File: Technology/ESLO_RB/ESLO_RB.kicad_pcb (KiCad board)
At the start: 4 copper layers, 48.8 x 20 mm, 71 parts, among them J1 Board to Board, J2 Conn_01x10_Female, U1 TPS62740, U10 MT29F2G01ABBGDWB-IT:G TR, U2 LP5907MFX-1.5, U3 CC2652RB, U4 2450BM14G0011, U5 MAX1720, U6 TPS72301DDCT, U7 ADS1294, U8 LSM303AGR, U9 CY15V104QI-20LPXC

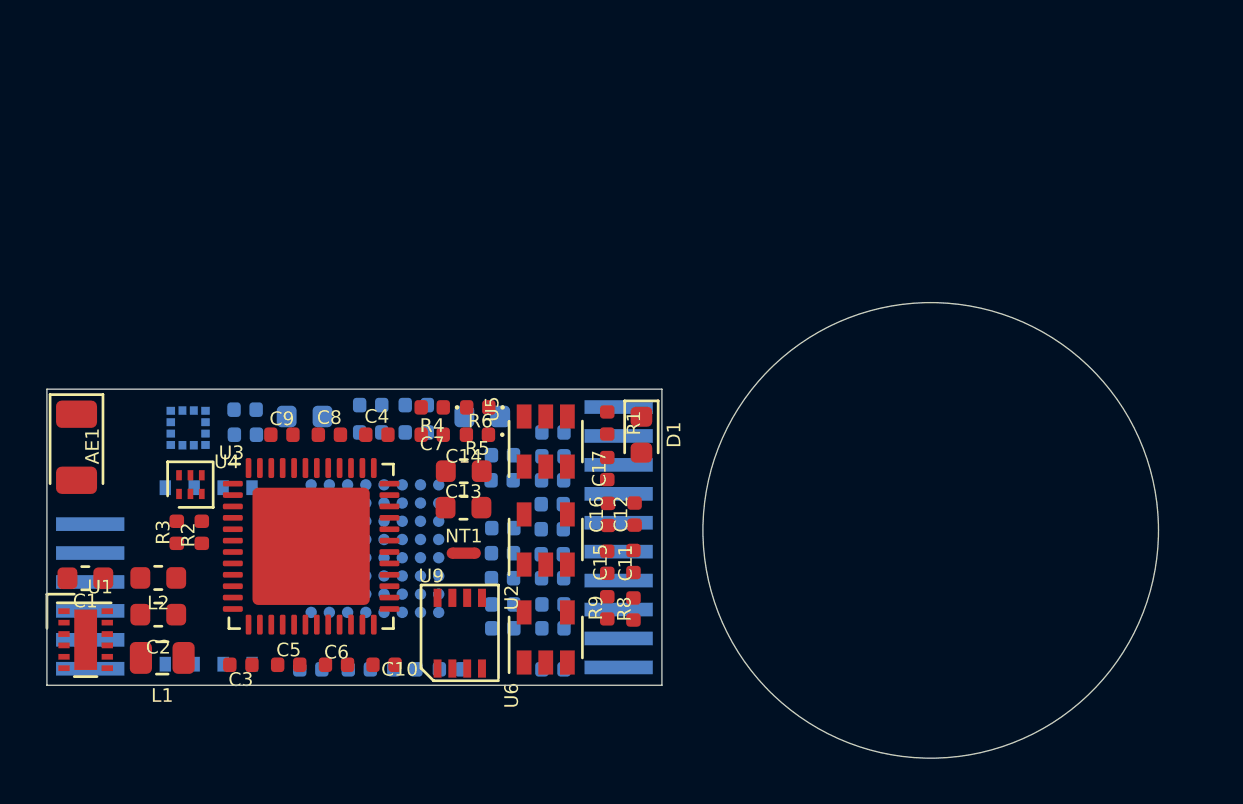
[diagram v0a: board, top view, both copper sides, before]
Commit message: Redo ESLO_RB with AC coupling
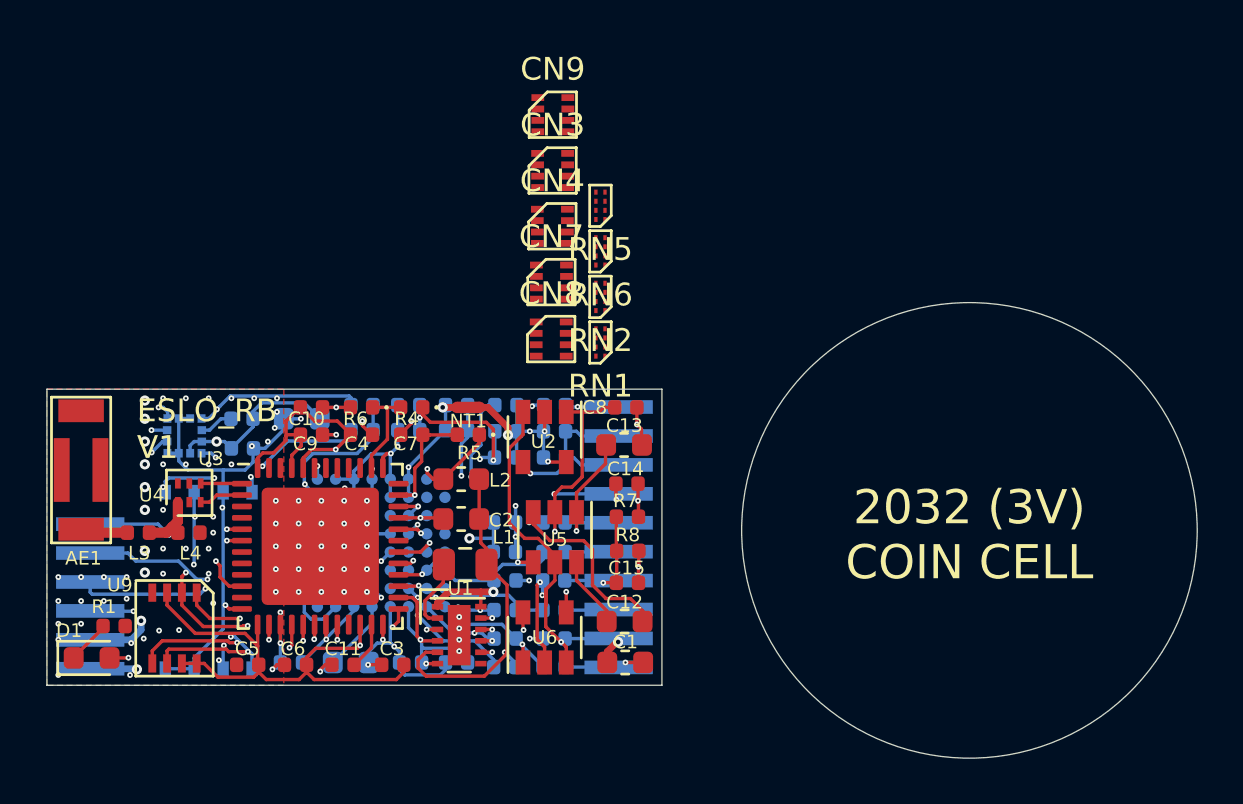
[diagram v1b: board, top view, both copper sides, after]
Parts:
- removed the C14 at (142.8, 93.3)
- removed the C23 at (140.7, 91.6)
- removed the C27 at (144.5, 93.7)
- removed the C36 at (146.7, 100.2)
- removed C37, C38: 1uF, Capacitor_SMD:C_0402_1005Metric
- removed the C9 at (134.8, 91.7)
- removed R17, R18: 4.7k, Resistor_SMD:R_0402_1005Metric
- removed the R7 at (146.7, 102.0)
- added C16: 1uF, Capacitor_SMD:C_0402_1005Metric, B.Cu at (140.4, 91.5)
- added C24: 4.7nF, Capacitor_SMD:C_0402_1005Metric, B.Cu at (144.6, 99.4)
- added C26: 0.1uF, Capacitor_SMD:C_0402_1005Metric, B.Cu at (133.1, 92.3)
- added C33: 0.1uF, Capacitor_SMD:C_0402_1005Metric, B.Cu at (144.6, 92.7)
- added C8: 1uF, Capacitor_SMD:C_0402_1005Metric, F.Cu at (149.9, 90.5)
- added CN3: 1000pF, ARBO Parts:0508_array, F.Cu at (146.7, 80.1)
- added CN4: 1uF, ARBO Parts:0508_array, F.Cu at (146.7, 82.5)
- added CN7: 1000pF, ARBO Parts:0508_array, F.Cu at (146.7, 85.0)
- added CN8: 1uF, ARBO Parts:0508_array, F.Cu at (146.6, 87.5)
- added CN9: 4700pF, ARBO Parts:0508_array, F.Cu at (146.7, 77.7)
- added L3: 3.3nH, Inductor_SMD:L_0402_1005Metric, F.Cu at (128.5, 96.0)
- added L4: 1.5nH, Inductor_SMD:L_0402_1005Metric, F.Cu at (130.7, 96.0)
- added R11: 100k, LED_SMD:LED_0402_1005Metric, B.Cu at (146.8, 90.4)
- added R13: 4.7k, Resistor_SMD:R_0402_1005Metric, B.Cu at (146.8, 99.4)
- added R9: 4.7k, Resistor_SMD:R_0402_1005Metric, B.Cu at (146.8, 96.8)
- added RN1: 4.7k, ARBO Parts:0502_array, F.Cu at (148.8, 87.7)
- added RN2: 1M, ARBO Parts:0502_array, F.Cu at (148.8, 85.7)
- added RN5: 4.7k, ARBO Parts:0502_array, F.Cu at (148.8, 81.7)
- added RN6: 1M, ARBO Parts:0502_array, F.Cu at (148.8, 83.7)
- AE1: footprint RF_Antenna:Johanson_2450AT18x100 -> ARBO Parts:2450AT42B100
- C10: value 1uF -> 100nF
- C12: value 1uF -> 10uF; footprint Capacitor_SMD:C_0402_1005Metric -> Capacitor_SMD:C_0603_1608Metric
- C15: value 2.2uF -> 10nF
- C17: value 10nF -> 0.1uF; moved to B.Cu
- C22: value 1uF -> 4.7nF
- C28: value 4.7nF -> 1uF
- C31: value 1uF -> 22uF; footprint Capacitor_SMD:C_0402_1005Metric -> Capacitor_SMD:C_0603_1608Metric
- C32: value 0.1uF -> 1uF
- C34: value 22uF -> 1uF; footprint Capacitor_SMD:C_0603_1608Metric -> Capacitor_SMD:C_0402_1005Metric
- R2, R3: moved to B.Cu
- moved D1 26.1 mm to (126.5, 101.5), turned to 0 degrees
- moved C1 24.0 mm to (149.9, 101.7)
- moved R1 23.4 mm to (127.5, 100.1), turned to 0 degrees
- moved U1 16.4 mm to (142.6, 100.5)
- moved C36 14.4 mm to (144.7, 90.4)
- moved L2 14.0 mm to (142.7, 93.7)
- moved C2 13.9 mm to (142.7, 95.4), turned to 0 degrees
- moved L1 13.9 mm to (142.9, 97.4), turned to 0 degrees
- moved C29 13.6 mm to (146.8, 91.5)
- moved C11 13.5 mm to (137.5, 101.8), turned to 0 degrees
- moved U9 12.5 mm to (130.1, 100.1), turned to 180 degrees
- moved R10 12.4 mm to (142.5, 90.4)
- moved C35 11.9 mm to (144.6, 101.9)
- moved C32 11.8 mm to (135.2, 101.7), turned to 180 degrees
- moved C10 11.7 mm to (136.1, 90.5)
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- renumbered C16 to C14, C26 to C23, C30 to C27, C33 to C30, C39 to C36, C8 to C9, R13 to R10, R8 to R7, R9 to R8
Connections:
- C10 pad 1: GNDD -> VDD
- C10 pad 2: Net-(C10-Pad2) -> GNDD
- C11 pad 1: GNDA -> GNDD
- C11 pad 2: +1V8 -> Net-(C11-Pad2)
- C12 pad 1: VDDA -> Net-(C12-Pad1)
- C12 pad 2: GNDA -> Net-(C12-Pad2)
- C13 pad 2: Net-(C13-Pad2) -> GNDA
- C15 pad 1: Net-(C14-Pad1) -> GNDA
- C15 pad 2: GNDA -> Net-(C15-Pad2)
- C17 pad 1: GNDA -> VDDA
- C17 pad 2: Net-(C17-Pad2) -> GNDA
- C18 pad 1: VDDA -> GNDD
- C18 pad 2: GNDA -> +1V8
- C19 pad 1: VDDA -> GNDD
- C19 pad 2: GNDA -> +1V8
- C20 pad 1: GNDA -> VSSA
- C20 pad 2: +1V8 -> Net-(C20-Pad2)
- C21 pad 1: GNDA -> VSSA
- C21 pad 2: +1V8 -> Net-(C20-Pad2)
- C22 pad 1: VSSA -> Net-(C22-Pad1)
- C28 pad 1: Net-(C28-Pad1) -> VSSA
- C28 pad 2: Net-(C28-Pad2) -> GNDA
- C29 pad 1: VDD -> VSSA
- C29 pad 2: GNDD -> GNDA
- C31 pad 1: VSSA -> Net-(C31-Pad1)
- C31 pad 2: GNDA -> VSSA
- C32 pad 1: VSSA -> Net-(C32-Pad1)
- C32 pad 2: GNDA -> VSSA
- C34 pad 1: Net-(C34-Pad1) -> Net-(C33-Pad1)
- J1 pad 6: (no net) -> DEBUG
- J2 pad 8: (no net) -> GNDA
- R12 pad 1: Net-(C25-Pad1) -> Net-(C22-Pad2)
- R12 pad 2: Net-(J2-Pad5) -> Net-(J2-Pad6)
- R14 pad 1: Net-(C25-Pad2) -> Net-(C24-Pad2)
- R14 pad 2: Net-(J2-Pad6) -> Net-(J2-Pad4)
- R15 pad 1: Net-(C27-Pad1) -> Net-(C25-Pad1)
- R15 pad 2: Net-(J2-Pad3) -> Net-(J2-Pad1)
- R16 pad 1: Net-(C27-Pad2) -> Net-(C25-Pad2)
- R16 pad 2: Net-(J2-Pad4) -> Net-(J2-Pad2)
- R7 pad 2: Net-(C17-Pad2) -> Net-(C15-Pad2)
- R8 pad 1: Net-(C17-Pad2) -> Net-(C15-Pad2)
- U10 pad 1: (no net) -> _NAND_CS
- U10 pad 6: SCK -> SCLK
- U3 pad 10: (no net) -> _AXY_MAG
- U3 pad 14: EEG_MISO -> MISO
- U3 pad 15: EEG_MOSI -> MOSI
- U3 pad 16: (no net) -> SCLK
- U3 pad 17: (no net) -> _FRAM_CS
- U3 pad 18: (no net) -> AXY_INT1
- U3 pad 19: (no net) -> AXY_INT2
- U3 pad 20: (no net) -> DEBUG
- U3 pad 23: Net-(C10-Pad2) -> Net-(C11-Pad2)
- U3 pad 26: (no net) -> ~SHDN
- U3 pad 27: (no net) -> EEG_MISO
- U3 pad 28: (no net) -> EEG_MOSI
- U3 pad 29: (no net) -> EEG_SCLK
- U3 pad 30: (no net) -> _NAND_CS
- U3 pad 32: (no net) -> EEG_START
- U3 pad 36: R_VBATT -> (no net)
- U3 pad 38: (no net) -> R_VBATT
- U4 pad 1: Net-(AE1-Pad1) -> Net-(L3-Pad1)
- U5 pad 1: Net-(C14-Pad1) -> Net-(C13-Pad1)
- U5 pad 3: Net-(C13-Pad2) -> Net-(C12-Pad2)
- U5 pad 6: Net-(C13-Pad1) -> Net-(C12-Pad1)
- U6 pad 2: Net-(C14-Pad1) -> Net-(C13-Pad1)
- U6 pad 4: Net-(C17-Pad2) -> Net-(C15-Pad2)
- U7 pad 1F: Net-(C25-Pad1) -> Net-(C22-Pad1)
- U7 pad 1G: Net-(C27-Pad1) -> Net-(C24-Pad1)
- U7 pad 1H: Net-(C28-Pad1) -> Net-(C25-Pad1)
- U7 pad 2F: Net-(C25-Pad2) -> Net-(C22-Pad2)
- U7 pad 2G: Net-(C27-Pad2) -> Net-(C24-Pad2)
- U7 pad 2H: Net-(C28-Pad2) -> Net-(C25-Pad2)
- U7 pad 3G: Net-(C38-Pad1) -> Net-(C35-Pad1)
- U7 pad 3H: Net-(C22-Pad2) -> Net-(C20-Pad2)
- U7 pad 5H: Net-(C34-Pad1) -> Net-(C31-Pad1)
- U7 pad 6H: Net-(C35-Pad1) -> Net-(C32-Pad1)
- U7 pad 7B: Net-(C36-Pad1) (its old number) -> Net-(C33-Pad1)
- U7 pad 7G: (no net) -> EEG_START
- U7 pad 8F: (no net) -> EEG_SCLK
- U8 pad 11: (no net) -> AXY_INT2
- U8 pad 12: (no net) -> AXY_INT1
- U8 pad 7: (no net) -> _AXY_MAG
- U9 pad 1: (no net) -> _FRAM_CS
- U9 pad 6: SCK -> SCLK
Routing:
- net VDD: track 0.00 -> 86.7 mm, vias 0 -> 6
- net +BATT: track 0.00 -> 45.1 mm, vias 0 -> 5
- net GNDD: track 0.00 -> 44.8 mm, vias 0 -> 106
- net +1V8: track 0.00 -> 41.2 mm, vias 0 -> 7
- net ~SHDN: track 0.00 -> 28.1 mm, vias 0 -> 4
- net VSSA: track 0.00 -> 22.1 mm, vias 0 -> 10
- net GNDA: track 0.00 -> 21.7 mm, vias 0 -> 11
- net _RESET: track 0.00 -> 21.5 mm, vias 0 -> 3
- net VDDA: track 0.00 -> 16.8 mm, vias 0 -> 3
- net _NAND_CS: track 0.00 -> 16.3 mm, vias 0 -> 3
- net SDA: track 0.00 -> 16.1 mm, vias 0 -> 3
- net JTAG_TCKC: track 0.00 -> 15.9 mm, vias 0 -> 3
- net JTAG_TMSC: track 0.00 -> 15.5 mm, vias 0 -> 3
- net SCL: track 0.00 -> 15.2 mm, vias 0 -> 4
- net DEBUG: track 0.00 -> 15.1 mm, vias 0 -> 3
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- added copper zone on GNDD, net GNDA
- added copper zone on F.Cu, net GNDD
- added copper zone on GNDD, net GNDD
- added copper zone on VSSA, net GNDD
- added copper zone on VSSA, net VSSA
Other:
- board size 48.8 x 20 mm -> 50.5 x 20 mm
- rule via_min_size: 0.254 -> 0.1
- board text added: "2032 (3V) COIN CELL"
- board text added: "ESLO_RB V1"

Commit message: Completed RB design
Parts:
- removed C18, C28: 1uF, Capacitor_SMD:C_0402_1005Metric
- removed C22, C24, C25: 4.7nF, Capacitor_SMD:C_0402_1005Metric
- removed C23: 1000pF, Capacitor_SMD:C_0402_1005Metric
- removed C27: 10uF, Capacitor_SMD:C_0603_1608Metric
- removed R1, R12, R13, R14, R15, R16, R9: 4.7k, Resistor_SMD:R_0402_1005Metric
- removed R10: 1M, Resistor_SMD:R_0402_1005Metric
- CN3, CN4, CN7, CN8, CN9, RN1, RN2, RN5, RN6: moved to B.Cu
- moved RN6 18.2 mm to (144.3, 101.3)
- moved RN5 17.2 mm to (146.9, 98.8), turned to 270 degrees
- moved CN7 16.3 mm to (146.3, 101.3)
- moved CN3 16.1 mm to (146.3, 96.2)
- moved CN9 13.5 mm to (146.5, 91.1), turned to 90 degrees
- moved C19 12.2 mm to (133.1, 92.6)
- moved RN2 11.5 mm to (144.3, 96.2)
- moved CN8 11.4 mm to (144.9, 98.8)
- moved CN4 11.2 mm to (144.9, 93.7)
- moved C35 10.7 mm to (141.8, 91.5), turned to 180 degrees
- moved RN1 6.28 mm to (146.9, 93.7), turned to 270 degrees
- moved C29 5.11 mm to (141.8, 90.4)
- moved C33 5.01 mm to (139.8, 91.5)
- moved C34 5.00 mm to (139.8, 90.4)
- moved R2 3.10 mm to (135.2, 90.4)
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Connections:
- CN3 pad 1: (no net) -> Net-(CN3-Pad1)
- CN3 pad 2: (no net) -> Net-(CN3-Pad2)
- CN3 pad 3: (no net) -> Net-(CN3-Pad3)
- CN3 pad 4: (no net) -> Net-(CN3-Pad4)
- CN3 pad 5: (no net) -> VSSA
- CN3 pad 6: (no net) -> VSSA
- CN3 pad 7: (no net) -> VSSA
- CN3 pad 8: (no net) -> VSSA
- CN4 pad 1: (no net) -> Net-(CN3-Pad1)
- CN4 pad 2: (no net) -> Net-(CN3-Pad2)
- CN4 pad 3: (no net) -> Net-(CN3-Pad3)
- CN4 pad 4: (no net) -> Net-(CN3-Pad4)
- CN4 pad 5: (no net) -> Net-(CN4-Pad5)
- CN4 pad 6: (no net) -> Net-(CN4-Pad6)
- CN4 pad 7: (no net) -> Net-(CN4-Pad7)
- CN4 pad 8: (no net) -> Net-(CN4-Pad8)
- CN7 pad 1: (no net) -> Net-(CN7-Pad1)
- CN7 pad 2: (no net) -> Net-(CN7-Pad2)
- CN7 pad 3: (no net) -> Net-(CN7-Pad3)
- CN7 pad 4: (no net) -> Net-(CN7-Pad4)
- CN7 pad 5: (no net) -> VSSA
- CN7 pad 6: (no net) -> VSSA
- CN7 pad 7: (no net) -> VSSA
- CN7 pad 8: (no net) -> VSSA
- CN8 pad 1: (no net) -> Net-(CN7-Pad1)
- CN8 pad 2: (no net) -> Net-(CN7-Pad2)
- CN8 pad 3: (no net) -> Net-(CN7-Pad3)
- CN8 pad 4: (no net) -> Net-(CN7-Pad4)
- CN8 pad 5: (no net) -> Net-(CN8-Pad5)
- CN8 pad 6: (no net) -> Net-(CN8-Pad6)
- CN8 pad 7: (no net) -> Net-(CN8-Pad7)
- CN8 pad 8: (no net) -> Net-(CN8-Pad8)
- CN9 pad 1: (no net) -> Net-(CN3-Pad2)
- CN9 pad 2: (no net) -> Net-(CN3-Pad3)
- CN9 pad 3: (no net) -> Net-(CN7-Pad1)
- CN9 pad 4: (no net) -> Net-(CN7-Pad3)
- CN9 pad 5: (no net) -> Net-(CN7-Pad4)
- CN9 pad 6: (no net) -> Net-(CN7-Pad2)
- CN9 pad 7: (no net) -> Net-(CN3-Pad4)
- CN9 pad 8: (no net) -> Net-(CN3-Pad1)
- D1 pad 1: Net-(D1-Pad1) -> GNDD
- J2 pad 7: Net-(C23-Pad1) -> Net-(J2-Pad7)
- J2 pad 8: GNDA -> Net-(J2-Pad8)
- R2 pad 1: +1V8 -> VDD
- R3 pad 1: +1V8 -> VDD
- RN1 pad 1: (no net) -> Net-(J2-Pad8)
- RN1 pad 2: (no net) -> Net-(J2-Pad7)
- RN1 pad 3: (no net) -> Net-(J2-Pad6)
- RN1 pad 4: (no net) -> Net-(J2-Pad5)
- RN1 pad 5: (no net) -> Net-(CN3-Pad4)
- RN1 pad 6: (no net) -> Net-(CN3-Pad3)
- RN1 pad 7: (no net) -> Net-(CN3-Pad2)
- RN1 pad 8: (no net) -> Net-(CN3-Pad1)
- RN2 pad 1: (no net) -> Net-(CN4-Pad8)
- RN2 pad 2: (no net) -> Net-(CN4-Pad7)
- RN2 pad 3: (no net) -> Net-(CN4-Pad6)
- RN2 pad 4: (no net) -> Net-(CN4-Pad5)
- RN2 pad 5: (no net) -> Net-(RN2-Pad5)
- RN2 pad 6: (no net) -> Net-(RN2-Pad5)
- RN2 pad 7: (no net) -> Net-(RN2-Pad5)
- RN2 pad 8: (no net) -> Net-(RN2-Pad5)
- RN5 pad 1: (no net) -> Net-(J2-Pad4)
- RN5 pad 2: (no net) -> Net-(J2-Pad3)
- RN5 pad 3: (no net) -> Net-(J2-Pad2)
- RN5 pad 4: (no net) -> Net-(J2-Pad1)
- RN5 pad 5: (no net) -> Net-(CN7-Pad4)
- RN5 pad 6: (no net) -> Net-(CN7-Pad3)
- RN5 pad 7: (no net) -> Net-(CN7-Pad2)
- RN5 pad 8: (no net) -> Net-(CN7-Pad1)
- RN6 pad 1: (no net) -> Net-(CN8-Pad8)
- RN6 pad 2: (no net) -> Net-(CN8-Pad7)
- RN6 pad 3: (no net) -> Net-(CN8-Pad6)
- RN6 pad 4: (no net) -> Net-(CN8-Pad5)
- RN6 pad 5: (no net) -> Net-(RN2-Pad5)
- RN6 pad 6: (no net) -> Net-(RN2-Pad5)
- RN6 pad 7: (no net) -> Net-(RN2-Pad5)
- RN6 pad 8: (no net) -> Net-(RN2-Pad5)
- U7 pad 1E: (no net) -> Net-(CN4-Pad8)
- U7 pad 1F: Net-(C22-Pad1) -> Net-(CN4-Pad6)
- U7 pad 1G: Net-(C24-Pad1) -> Net-(CN8-Pad8)
- U7 pad 1H: Net-(C25-Pad1) -> Net-(CN8-Pad6)
- U7 pad 2E: (no net) -> Net-(CN4-Pad7)
- U7 pad 2F: Net-(C22-Pad2) -> Net-(CN4-Pad5)
- U7 pad 2G: Net-(C24-Pad2) -> Net-(CN8-Pad7)
- U7 pad 2H: Net-(C25-Pad2) -> Net-(CN8-Pad5)
- U7 pad 3A: Net-(C23-Pad1) -> VDDA
- U7 pad 3B: Net-(C23-Pad1) -> Net-(RN2-Pad5)
- U7 pad 3C: Net-(C23-Pad2) -> Net-(RN2-Pad5)
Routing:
- net Net-(CN7-Pad4): track 0.00 -> 16.2 mm, vias 0 -> 3
- net Net-(CN7-Pad2): track 0.00 -> 15.8 mm, vias 0 -> 3
- net Net-(CN7-Pad1): track 0.00 -> 15.8 mm, vias 0 -> 2
- net Net-(CN7-Pad3): track 0.00 -> 14.6 mm, vias 0 -> 3
- net Net-(C23-Pad1): track 14.4 -> 0.00 mm, vias 2 -> 0
- net Net-(RN2-Pad5): track 0.00 -> 13.6 mm, vias 0 -> 2
- net Net-(CN3-Pad4): track 0.00 -> 12.1 mm, vias 0 -> 2
- net VSSA: track 22.1 -> 32.9 mm, vias 10 -> 14
- net Net-(C22-Pad2): track 9.81 -> 0.00 mm, vias 3 -> 0
- net Net-(CN3-Pad3): track 0.00 -> 9.12 mm, vias 0 -> 2
- net Net-(CN3-Pad2): track 0.00 -> 7.16 mm, vias 0 -> 2
- net Net-(CN4-Pad7): track 0.00 -> 7.02 mm, vias 0 -> 2
- net Net-(C24-Pad2): track 7.00 -> 0.00 mm, vias 4 -> 0
- net Net-(C25-Pad2): track 6.75 -> 0.00 mm, vias 2 -> 0
- net Net-(CN4-Pad8): track 0.00 -> 6.68 mm
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
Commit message: Checked all pins, ready for production
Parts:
- AE1: value Antenna -> 2450AT42B100
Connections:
- net DEBUG renamed _DEBUG
- U3 pad 31: (no net) -> _EEG_CS
- U3 pad 36: (no net) -> _EEG_DRDY
- U7 pad 6D: (no net) -> _EEG_DRDY
- U7 pad 7F: (no net) -> _EEG_CS
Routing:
- net _EEG_CS: track 0.00 -> 4.98 mm, vias 0 -> 3
- net _EEG_DRDY: track 0.00 -> 4.34 mm, vias 0 -> 3
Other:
- board size 50.5 x 20 mm -> 27 x 13 mm
- board text removed: "2032 (3V) COIN CELL"

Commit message: Submit ESLO_RB for mfg w PCBONLINE
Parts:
- removed the C20 at (140.5, 101.7)
- removed the C21 at (142.5, 101.7)
- removed C31: 22uF, Capacitor_SMD:C_0603_1608Metric
- removed C32: 1uF, Capacitor_SMD:C_0402_1005Metric
- removed the R6 at (138.3, 90.5)
- added C13: 22uF, Capacitor_SMD:C_0603_1608Metric, B.Cu at (138.0, 101.7)
- added C14: 1uF, Capacitor_SMD:C_0402_1005Metric, B.Cu at (135.5, 101.7)
- added C24: 1uF, Capacitor_SMD:C_0402_1005Metric, B.Cu at (140.6, 101.7)
- added C27: 0.1uF, Capacitor_SMD:C_0402_1005Metric, B.Cu at (142.5, 101.7)
- added R2: 100k, LED_SMD:LED_0402_1005Metric, F.Cu at (138.3, 90.5)
- C11: renamed from C7; value 100nF -> 0.1uF
- C22: renamed from C10; value 100nF -> 0.1uF
- C25: renamed from C9; value 100nF -> 0.1uF
- C26: renamed from C6; value 100nF -> 0.1uF
- C28: renamed from C5; value 100nF -> 0.1uF
- C29: renamed from C4; value 100nF -> 0.1uF
- C7: renamed from C30; value 220nF -> 0.22uF
- J1: renamed from J2; value Conn_01x10_Female -> 10POS Biopotentials
- J2: renamed from J1; value Board to Board -> 6POS Power/JTAG
- moved U7 0.30 mm to (131.3, 98.0)
- renumbered C15 to C10, C14 to C12, C33 to C15, C34 to C16, C35 to C18, C36 to C19, C12 to C2, C19 to C20, C11 to C21, C29 to C23, C26 to C3, C13 to C4, C8 to C5, C2 to C6, C3 to C8, C16 to C9, CN9 to CN1, CN3 to CN2, CN7 to CN3, CN8 to CN5, L4 to L3, L3 to L4, R4 to R1, R5 to R3, R7 to R4, R8 to R5, R2 to R6, R3 to R7, R11 to R8, RN5 to RN2, RN2 to RN3, RN6 to RN4, U5 to U1, U4 to U10, U1 to U2, U9 to U3, U8 to U4, U2 to U5, U10 to U7, U3 to U8, U7 to U9
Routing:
- net VDD: track 90.6 -> 91.2 mm
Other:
- rule trace_min: 0.15 -> 0.12

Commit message: Assembling ESLO_RB
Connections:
- U2 pad 7: (no net) -> _RESET
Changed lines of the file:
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@@
   (page A4)
   (layers
-    (0 F.Cu signal hide)
+    (0 F.Cu signal)
     (1 GNDD power hide)
     (2 VSSA power hide)
-    (31 B.Cu mixed)
+    (31 B.Cu mixed hide)
     (32 B.Adhes user hide)
     (33 F.Adhes user hide)
@@
     (35 F.Paste user hide)
     (36 B.SilkS user hide)
-    (37 F.SilkS user hide)
+    (37 F.SilkS user)
     (38 B.Mask user hide)
     (39 F.Mask user hide)
@@
     (45 Margin user hide)
     (46 B.CrtYd user hide)
-    (47 F.CrtYd user)
+    (47 F.CrtYd user hide)
     (48 B.Fab user hide)
     (49 F.Fab user hide)
@@
     (pad 8 smd rect (at 0.95 0.75) (size 0.5 0.25) (layers F.Cu F.Paste F.Mask)
       (net 3 GNDD))
-    (pad 7 smd rect (at 0.95 1.25) (size 0.5 0.25) (layers F.Cu F.Paste F.Mask))
+    (pad 7 smd rect (at 0.95 1.25) (size 0.5 0.25) (layers F.Cu F.Paste F.Mask)
+      (net 20 _RESET))
     (pad 6 smd rect (at -0.95 1.25) (size 0.5 0.25) (layers F.Cu F.Paste F.Mask)
       (net 6 +1V8))
